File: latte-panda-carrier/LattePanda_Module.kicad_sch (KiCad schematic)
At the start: 3 parts

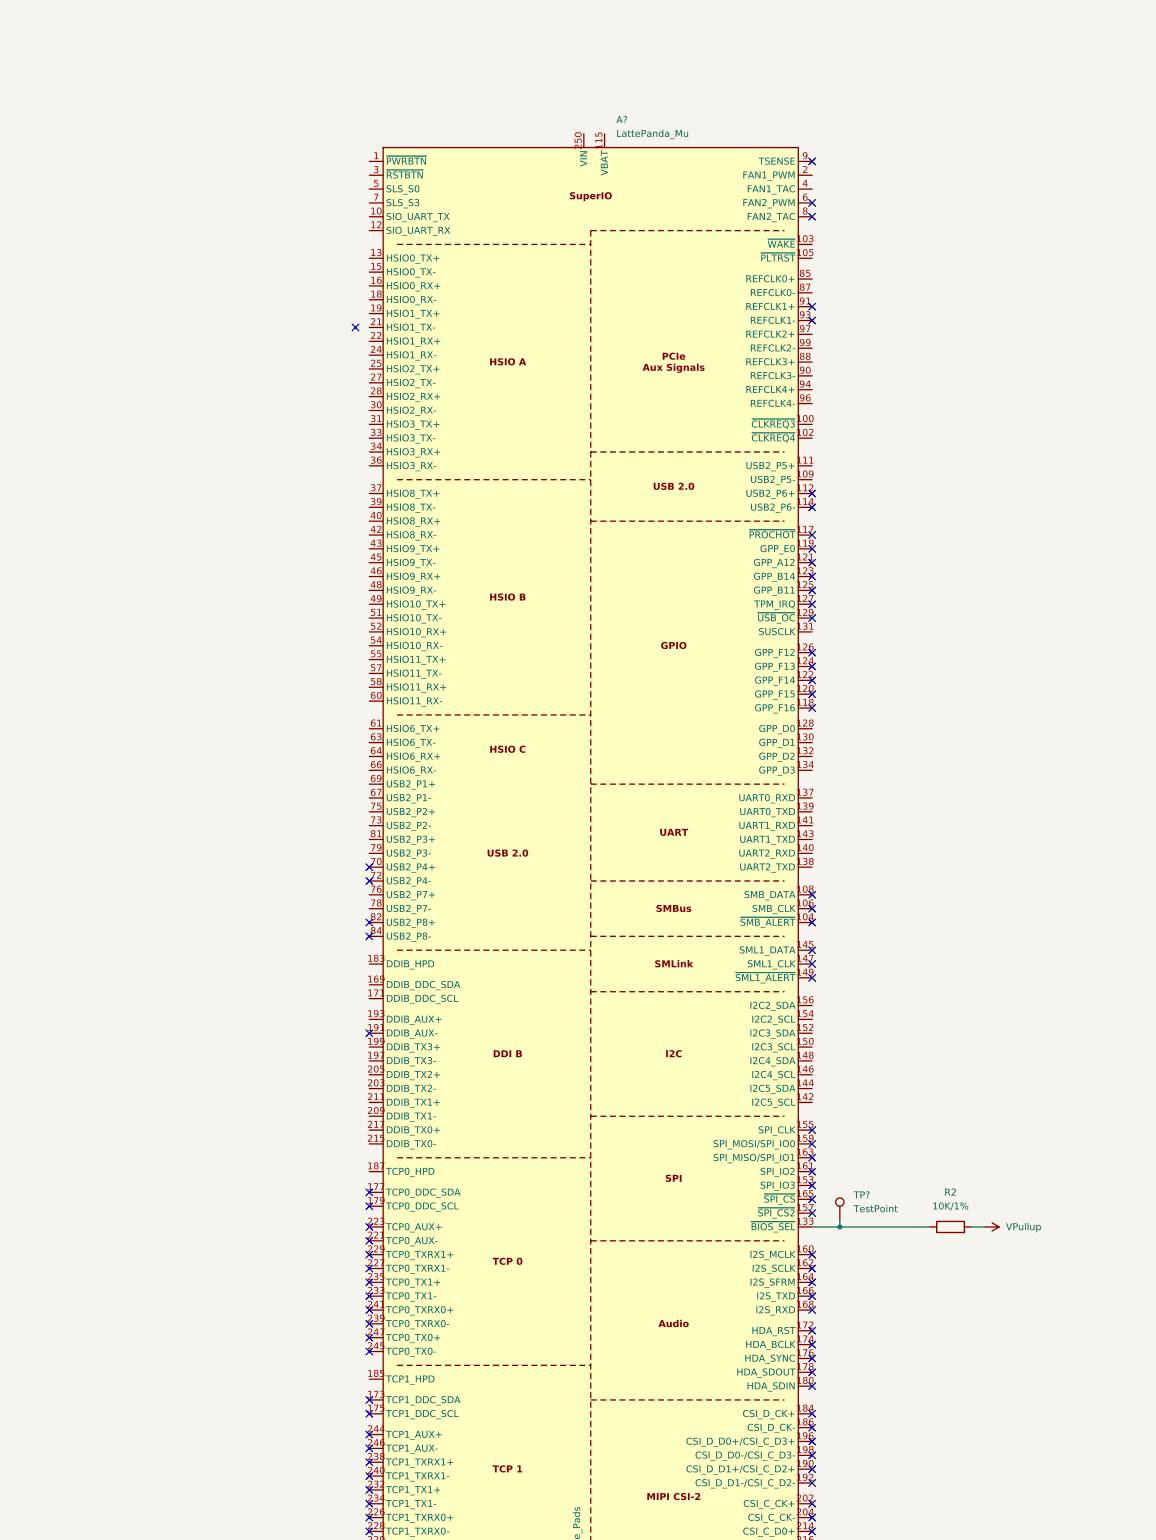
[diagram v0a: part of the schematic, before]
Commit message: 100.2
Added pull down resistors to LattePanda Mu -sheet.
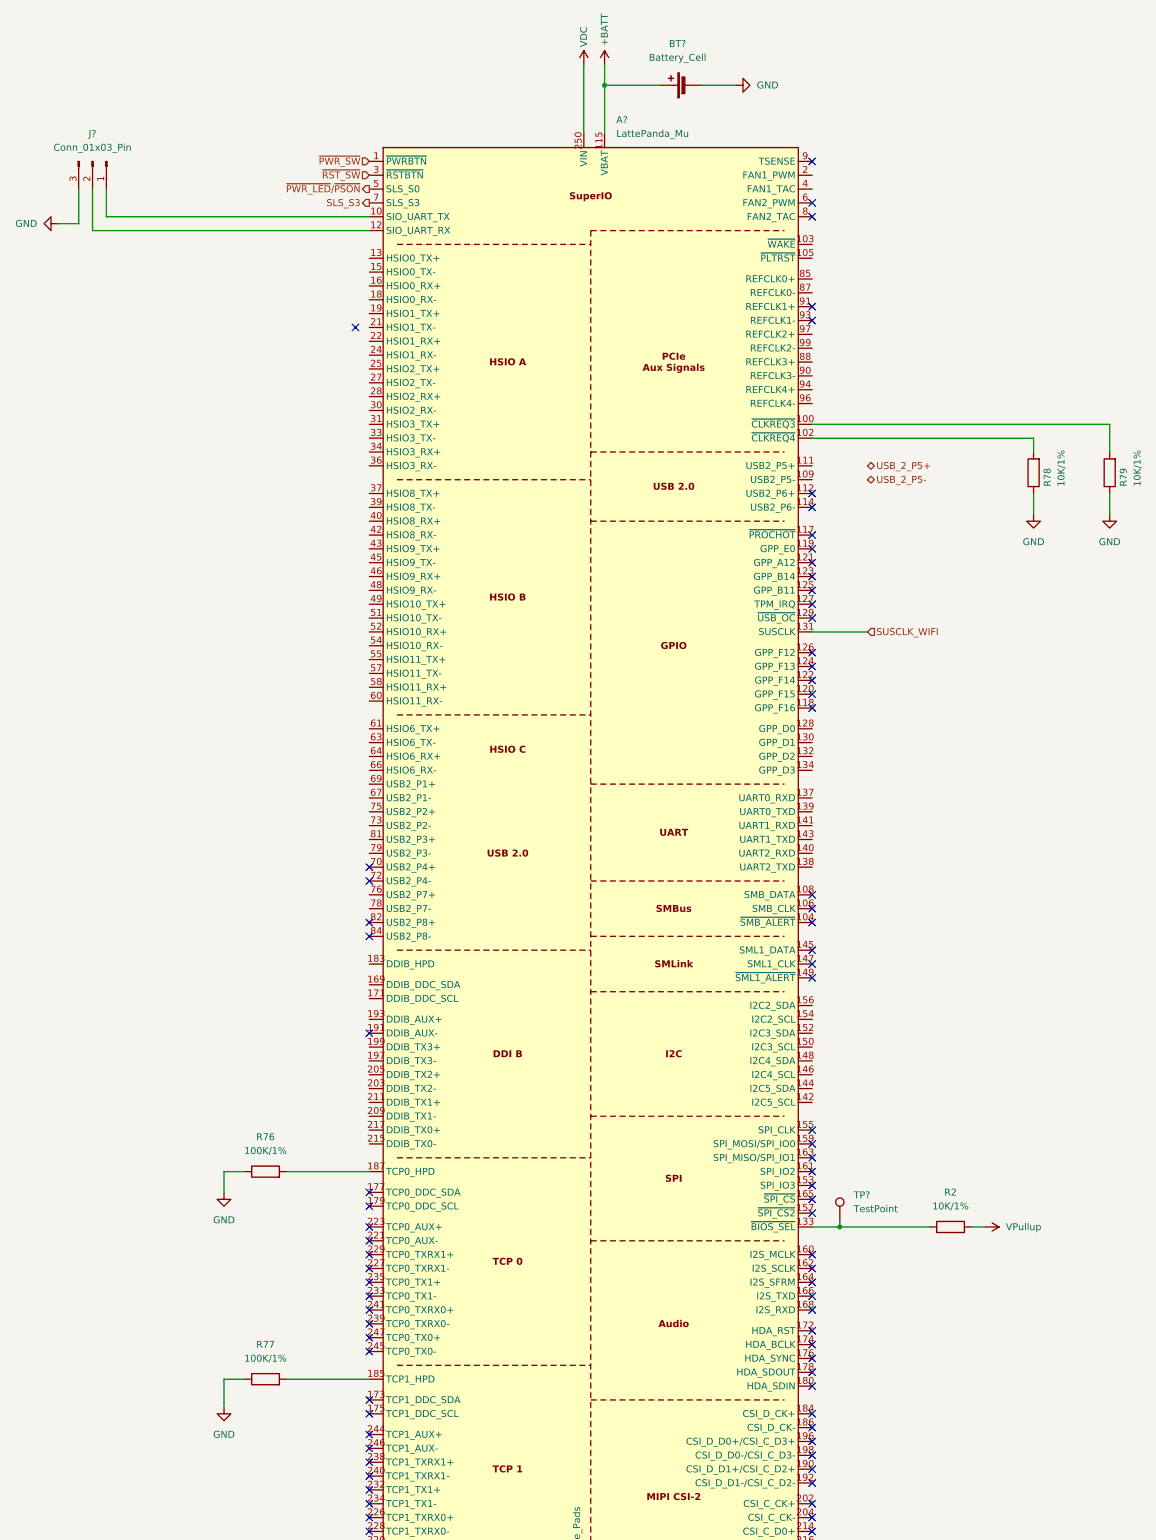
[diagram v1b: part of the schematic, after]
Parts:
- added BT?: Battery_Cell, symbol Device:Battery_Cell
- added J?: Conn_01x03_Pin, A_HDJ_Library:PinHeader_1x03_P2.54mm_Vertical, symbol Connector:Conn_01x03_Pin
- added R76, R77: 100K/1%, symbol Device:R
- added R78, R79: 10K/1%, symbol Device:R
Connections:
- net GND: now also BT?.2 (-), J?.3 (Pin_3), R76.1, R77.1, R78.1, R79.1
- net ~{PWR_SW}: now reaches A?.1 (~{PWRBTN})
- net at A?.10 (SIO_UART_TX): now also J?.1 (Pin_1)
- net at A?.100 (~{CLKREQ3}): now also R79.2
- net at A?.102 (~{CLKREQ4}): now also R78.2
- net +BATT: now reaches A?.115 (VBAT)
- net +BATT: now also BT?.1 (+)
- net at A?.12 (SIO_UART_RX): now also J?.2 (Pin_2)
- net SUSCLK_WIFI: now reaches A?.131 (SUSCLK)
- net at A?.185 (TCP1_HPD): now also R77.2
- net at A?.187 (TCP0_HPD): now also R76.2
- net VDC: now reaches A?.250 (VIN), A?.251 (VIN), A?.252 (VIN), A?.253 (VIN), A?.254 (VIN), A?.255 (VIN), A?.256 (VIN), A?.257 (VIN), A?.258 (VIN), A?.259 (VIN), A?.260 (VIN)
- net ~{RST_SW}: now reaches A?.3 (~{RSTBTN})
- net ~{PWR_LED}/~{PSON}: now reaches A?.5 (SLS_S0)
- net SLS_S3: now reaches A?.7 (SLS_S3)

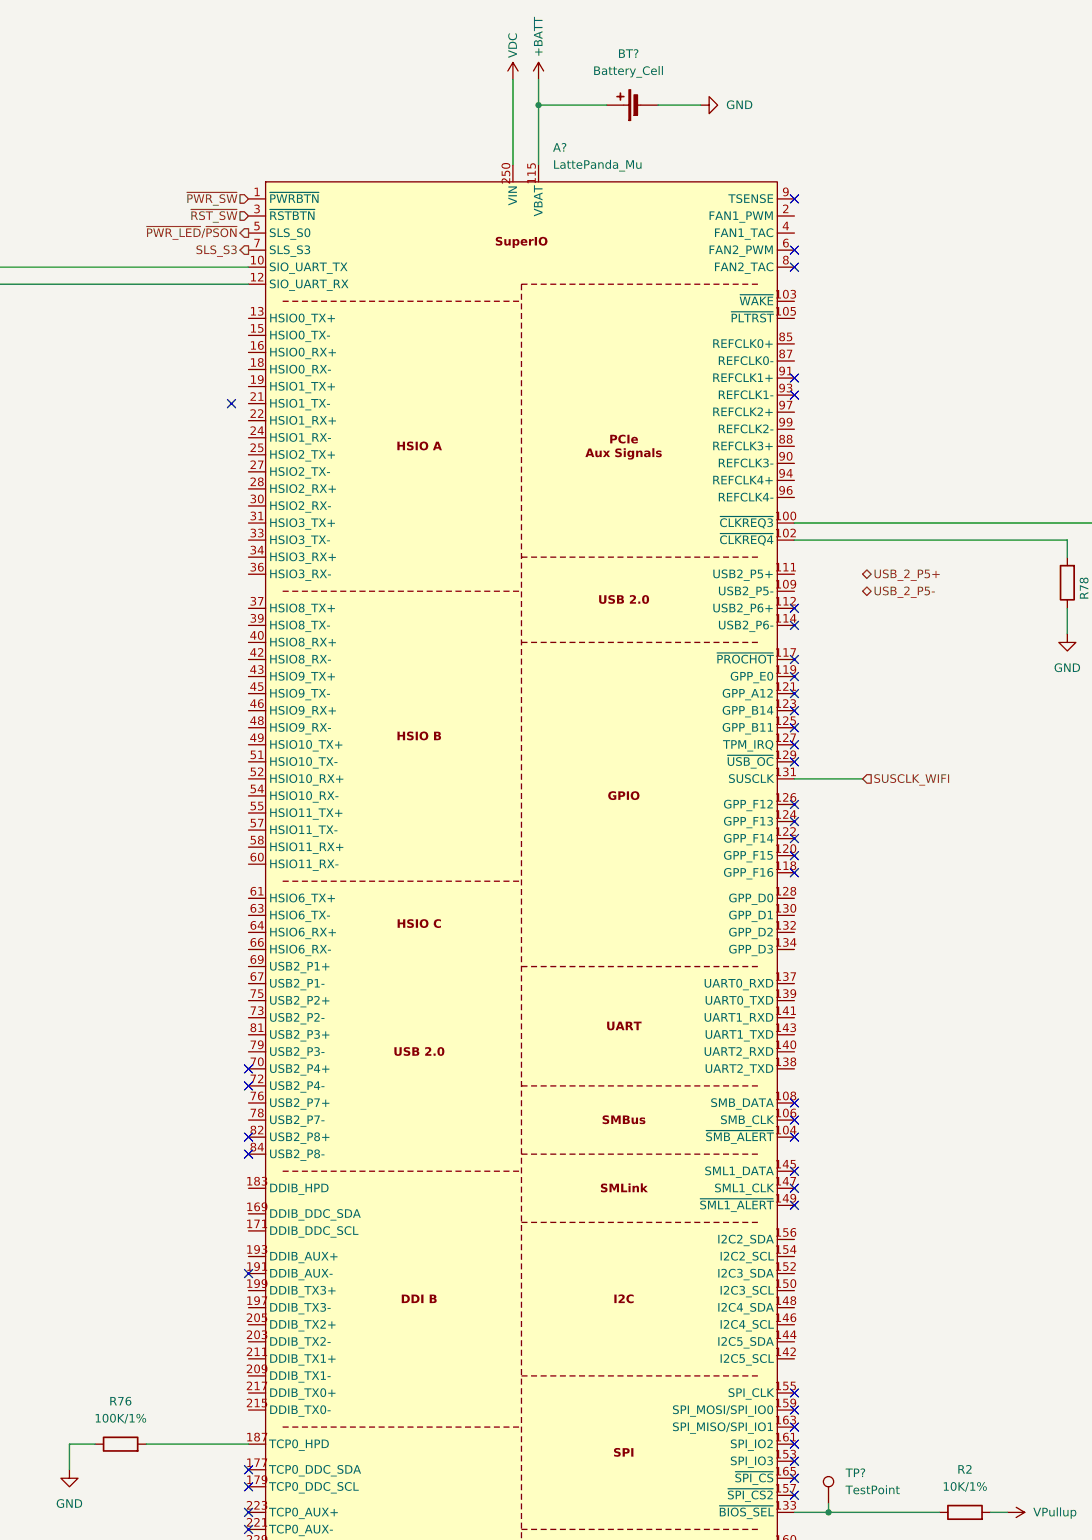
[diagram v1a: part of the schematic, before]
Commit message: 100.3
Hierarchical labels to LattePand Mu sheet.
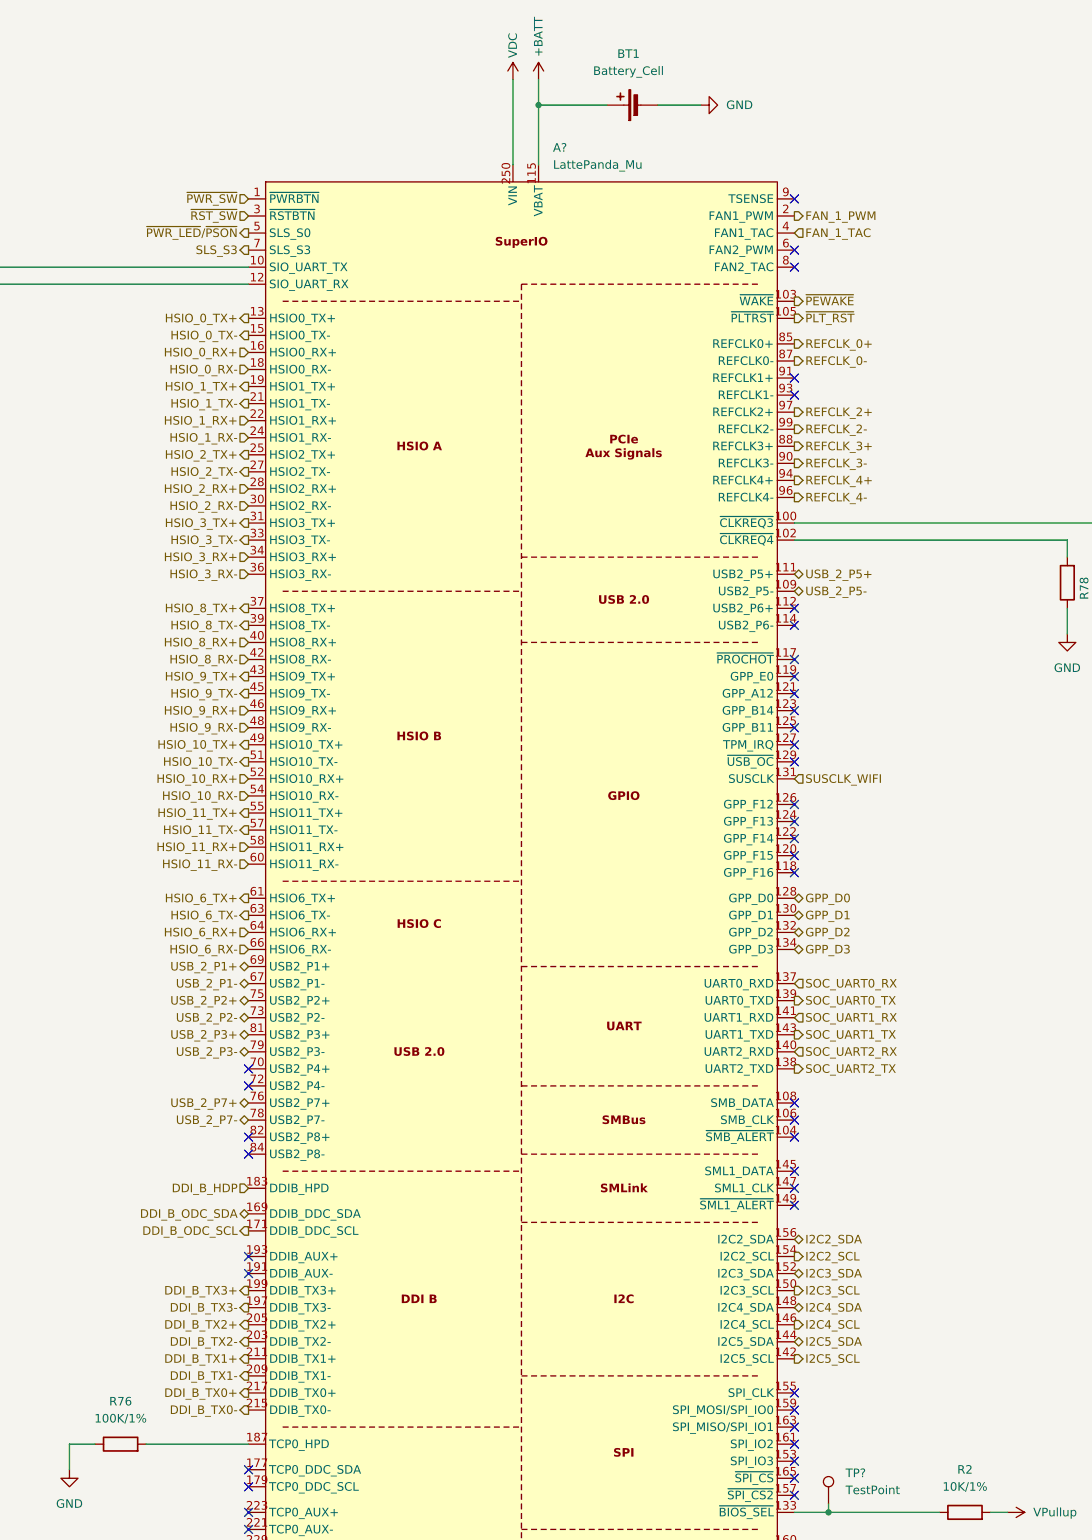
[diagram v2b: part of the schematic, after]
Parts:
- gave numbers to parts that had none: 1
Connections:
- net USB_2_P5+: now also A?.111 (USB2_P5+)
- net USB_2_P5-: now also A?.109 (USB2_P5-)
- net ~{PEWAKE}: now reaches A?.103 (~{WAKE})
- net ~{PLT_RST}: now reaches A?.105 (~{PLTRST})
- net GPP_D0: now reaches A?.128 (GPP_D0)
- net HSIO_0_TX+: now reaches A?.13 (HSIO0_TX+)
- net GPP_D1: now reaches A?.130 (GPP_D1)
- net GPP_D2: now reaches A?.132 (GPP_D2)
- net GPP_D3: now reaches A?.134 (GPP_D3)
- net SOC_UART0_RX: now reaches A?.137 (UART0_RXD)
- net SOC_UART2_TX: now reaches A?.138 (UART2_TXD)
- net SOC_UART0_TX: now reaches A?.139 (UART0_TXD)
- net SOC_UART2_RX: now reaches A?.140 (UART2_RXD)
- net SOC_UART1_RX: now reaches A?.141 (UART1_RXD)
- net I2C5_SCL: now reaches A?.142 (I2C5_SCL)
- net SOC_UART1_TX: now reaches A?.143 (UART1_TXD)
- net I2C5_SDA: now reaches A?.144 (I2C5_SDA)
- net I2C4_SCL: now reaches A?.146 (I2C4_SCL)
- net I2C4_SDA: now reaches A?.148 (I2C4_SDA)
- net HSIO_0_TX-: now reaches A?.15 (HSIO0_TX-)
- net I2C3_SCL: now reaches A?.150 (I2C3_SCL)
- net I2C3_SDA: now reaches A?.152 (I2C3_SDA)
- net I2C2_SCL: now reaches A?.154 (I2C2_SCL)
- net I2C2_SDA: now reaches A?.156 (I2C2_SDA)
- net HSIO_0_RX+: now reaches A?.16 (HSIO0_RX+)
- net DDI_B_ODC_SDA: now reaches A?.169 (DDIB_DDC_SDA)
- net DDI_B_ODC_SCL: now reaches A?.171 (DDIB_DDC_SCL)
- net HSIO_0_RX-: now reaches A?.18 (HSIO0_RX-)
- net DDI_B_HDP: now reaches A?.183 (DDIB_HPD)
- net HSIO_1_TX+: now reaches A?.19 (HSIO1_TX+)
- net DDI_B_TX3-: now reaches A?.197 (DDIB_TX3-)
- net DDI_B_TX3+: now reaches A?.199 (DDIB_TX3+)
- net FAN_1_PWM: now reaches A?.2 (FAN1_PWM)
- net DDI_B_TX2-: now reaches A?.203 (DDIB_TX2-)
- net DDI_B_TX2+: now reaches A?.205 (DDIB_TX2+)
- net DDI_B_TX1-: now reaches A?.209 (DDIB_TX1-)
- net HSIO_1_TX-: now reaches A?.21 (HSIO1_TX-)
- net DDI_B_TX1+: now reaches A?.211 (DDIB_TX1+)
- net DDI_B_TX0-: now reaches A?.215 (DDIB_TX0-)
- net DDI_B_TX0+: now reaches A?.217 (DDIB_TX0+)
- net HSIO_1_RX+: now reaches A?.22 (HSIO1_RX+)
- net HSIO_1_RX-: now reaches A?.24 (HSIO1_RX-)
- net HSIO_2_TX+: now reaches A?.25 (HSIO2_TX+)
- net HSIO_2_TX-: now reaches A?.27 (HSIO2_TX-)
- net HSIO_2_RX+: now reaches A?.28 (HSIO2_RX+)
- net HSIO_2_RX-: now reaches A?.30 (HSIO2_RX-)
- net HSIO_3_TX+: now reaches A?.31 (HSIO3_TX+)
- net HSIO_3_TX-: now reaches A?.33 (HSIO3_TX-)
- net HSIO_3_RX+: now reaches A?.34 (HSIO3_RX+)
- net HSIO_3_RX-: now reaches A?.36 (HSIO3_RX-)
- net HSIO_8_TX+: now reaches A?.37 (HSIO8_TX+)
- net HSIO_8_TX-: now reaches A?.39 (HSIO8_TX-)
- net FAN_1_TAC: now reaches A?.4 (FAN1_TAC)
- net HSIO_8_RX+: now reaches A?.40 (HSIO8_RX+)
- net HSIO_8_RX-: now reaches A?.42 (HSIO8_RX-)
- net HSIO_9_TX+: now reaches A?.43 (HSIO9_TX+)
- net HSIO_9_TX-: now reaches A?.45 (HSIO9_TX-)
- net HSIO_9_RX+: now reaches A?.46 (HSIO9_RX+)
- net HSIO_9_RX-: now reaches A?.48 (HSIO9_RX-)
- net HSIO_10_TX+: now reaches A?.49 (HSIO10_TX+)
- net HSIO_10_TX-: now reaches A?.51 (HSIO10_TX-)
- net HSIO_10_RX+: now reaches A?.52 (HSIO10_RX+)
- net HSIO_10_RX-: now reaches A?.54 (HSIO10_RX-)
- net HSIO_11_TX+: now reaches A?.55 (HSIO11_TX+)
- net HSIO_11_TX-: now reaches A?.57 (HSIO11_TX-)
- net HSIO_11_RX+: now reaches A?.58 (HSIO11_RX+)
- net HSIO_11_RX-: now reaches A?.60 (HSIO11_RX-)
- net HSIO_6_TX+: now reaches A?.61 (HSIO6_TX+)
- net HSIO_6_TX-: now reaches A?.63 (HSIO6_TX-)
- net HSIO_6_RX+: now reaches A?.64 (HSIO6_RX+)
- net HSIO_6_RX-: now reaches A?.66 (HSIO6_RX-)
- net USB_2_P1-: now reaches A?.67 (USB2_P1-)
- net USB_2_P1+: now reaches A?.69 (USB2_P1+)
- net USB_2_P2-: now reaches A?.73 (USB2_P2-)
- net USB_2_P2+: now reaches A?.75 (USB2_P2+)
- net USB_2_P7+: now reaches A?.76 (USB2_P7+)
- net USB_2_P7-: now reaches A?.78 (USB2_P7-)
- net USB_2_P3-: now reaches A?.79 (USB2_P3-)
- net USB_2_P3+: now reaches A?.81 (USB2_P3+)
- net REFCLK_0+: now reaches A?.85 (REFCLK0+)
- net REFCLK_0-: now reaches A?.87 (REFCLK0-)
- net REFCLK_3+: now reaches A?.88 (REFCLK3+)
- net REFCLK_3-: now reaches A?.90 (REFCLK3-)
- net REFCLK_4+: now reaches A?.94 (REFCLK4+)
- net REFCLK_4-: now reaches A?.96 (REFCLK4-)
- net REFCLK_2+: now reaches A?.97 (REFCLK2+)
- net REFCLK_2-: now reaches A?.99 (REFCLK2-)

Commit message: 100.4
Add LattePanda Mu -schematic pins.
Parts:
- gave numbers to parts that had none: 1
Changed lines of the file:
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@@
 		(dnp no)
 		(fields_autoplaced yes)
-		(property "Reference" "TP?"
+		(property "Reference" "TP7"
 			(at 334.01 264.6679 0)
 			(effects
@@
 			(project ""
 				(path "/9ba2df7d-1c0f-41ea-bb38-2c3f31e14521/b21888af-f6e8-4fba-8e9d-8ac96a3e6368"
-					(reference "TP?")
+					(reference "TP7")
 					(unit 1)
 				)

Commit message: 100.5
LattePanda Mu schematic sheet - On sheet documentation
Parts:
- renumbered BT1 to BT?, R2 to R?, R77 to R?, R78 to R?, R76 to R?, R79 to R?, TP7 to TP?
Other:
- note added: "All I2C have integrated pull-up resistors. no need to add pull-up resistors"
- note added: "DDI/TCP functions are defined by the BIOS source code, Cannot be changed in BIOS settings. Before starting design, you should choose one of the available BIOS configurations on: https://github.com/LattePandaTeam/LattePanda-Mu The default functions are defined as follows: - DDIA: eDP 1.4b (the 40Pin connector on the Mu) - DDIB: HDMI 2.0 - TCP0: HDMI 2.0 - TCP1: USB TypeC (need external PD controll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"
- note added: "HSIO functions are defined by the BIOS source code, Cannot be changed in BIOS settings. Before starting design, you should choose one of the available BIOS configurations on: https://github.com/LattePandaTeam/LattePanda-Mu Or contact techsupport for custom your BIOS The default functions are defined as follows: - HSIO0: USB3.2 10Gbps - HSIO1: USB3.2 10Gbps - HSIO2: PCIe 3.0 x1 - HSIO3: PCIe 3.0 x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"
- note added: "Lite Carrier has no second BIOS ROM ~{BIOS_SEL} pull up to 3.3V to select ROM on LattePanda Mu"
- note added: "SPI is only used to connect to the BIOS ROM and discrete TPM Cannot be used as a general SPI interface."
- note added: "Sleeping State Signal - SLS_S0: - S0 (Working): HIGH - S3 (Slpeeping): LOW - S4 (Hibernation): LOW - S5 (Soft Off): LOW - SLS_S3: - S0 (Working): HIGH - S3 (Slpeeping): HIGH - S4 (Hibernation): LOW - S5 (Soft Off): LOW"
- note added: "USB2_P6 is reserved for TypeC PD Controller DO NOT use it as a normal USB"
- note added: "~{CLKREQ} is reserved for PCIe ASPM L1s Unless the device clearly supports it, pull it down to enhance compatibility"
- moved on the sheet: J?, R?
